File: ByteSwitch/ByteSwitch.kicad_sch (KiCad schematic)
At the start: 12 parts, among them J1 Conn_01x08_Pin, J2 Conn_01x01_Socket, J3 Conn_01x01_Socket, SW1 SW_DIP_x08

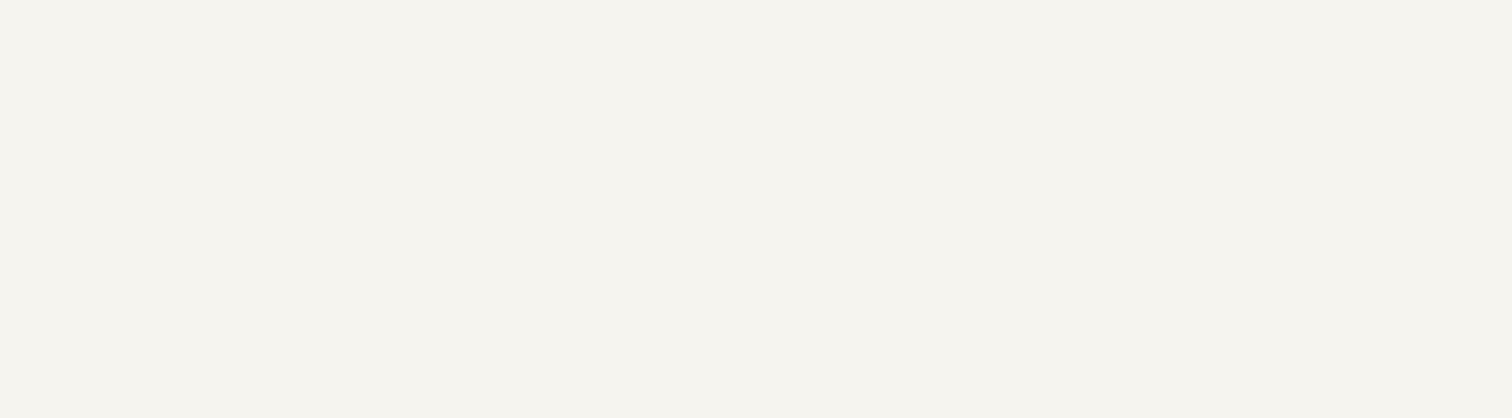
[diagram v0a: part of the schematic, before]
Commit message: Add pullup resistors to ClockGen and ByteHex
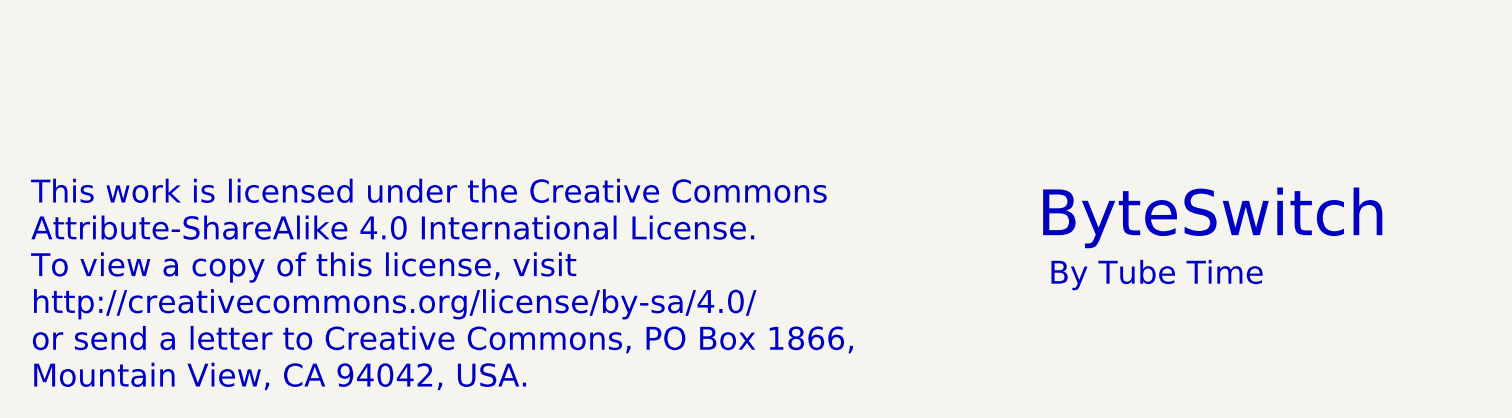
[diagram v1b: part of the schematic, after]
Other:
- note added: "By Tube Time"
- note added: "ByteSwitch"
- note added: "This work is licensed under the Creative Commons Attribute-ShareAlike 4.0 International License. To view a copy of this license, visit http://creativecommons.org/license/by-sa/4.0/ or send a letter to Creative Commons, PO Box 1866, Mountain View, CA 94042, USA."
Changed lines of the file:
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@@
     (stroke (width 0) (type default))
+  )
+  (text "By Tube Time" (at 180.34 179.07 0)
+    (effects (font (size 2.54 2.54)) (justify left bottom))
+  )
+  (text "ByteSwitch" (at 179.07 173.99 0)
+    (effects (font (size 5.08 5.08)) (justify left bottom))
+  )
+  (text "This work is licensed under the Creative Commons\nAttribute-ShareAlike 4.0 International License.\nTo view a copy of this license, visit\nhttp://creativecommons.org/license/by-sa/4.0/\nor send a letter to Creative Commons, PO Box 1866,\nMountain View, CA 94042, USA."
+    (at 67.31 190.5 0)
+    (effects (font (size 2.54 2.54)) (justify left bottom))
   )
   (symbol (lib_id "Device:R_Small_US") (at 95.25 97.79 0) (mirror x) (unit 1)
